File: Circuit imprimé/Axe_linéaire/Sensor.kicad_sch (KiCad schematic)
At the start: 0 parts

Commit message: Ajout de l'IMU + modèle du photointerrupteur
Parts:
- added C1, C2: 100n, symbol Device:C
- added JP1: SolderJumper_3_Bridged12, symbol Jumper:SolderJumper_3_Bridged12
- added JP2: SolderJumper_2_Open, symbol Jumper:SolderJumper_2_Open
- added R1: 10k, symbol Device:R
- added U2: LSM6DSRTR, Library:LGA-14_2.5X3X0.86_, symbol 2022-12-24_18-31-24:LSM6DSRTR
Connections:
- new net: JP2.1 (A), R1.2, U2.1 (SDO/SA0)
- new net: JP1.2 (C), U2.12 (CS)
- new net +3.3V: C1.1, C2.1, JP1.1 (A), R1.1, U2.5 (VDD_IO), U2.8 (VDD)
- new net GND: C1.2, C2.2, JP2.2 (B), U2.2 (SDX_), U2.3 (SCX), U2.6 (GND), U2.7 (GND)
- new net INT1_Bas: U2.4 (INT1)
- new net INT2_Bas: U2.9 (INT2)
- new net SCL: U2.13 (SCL)
- new net SDA: U2.14 (SDA)

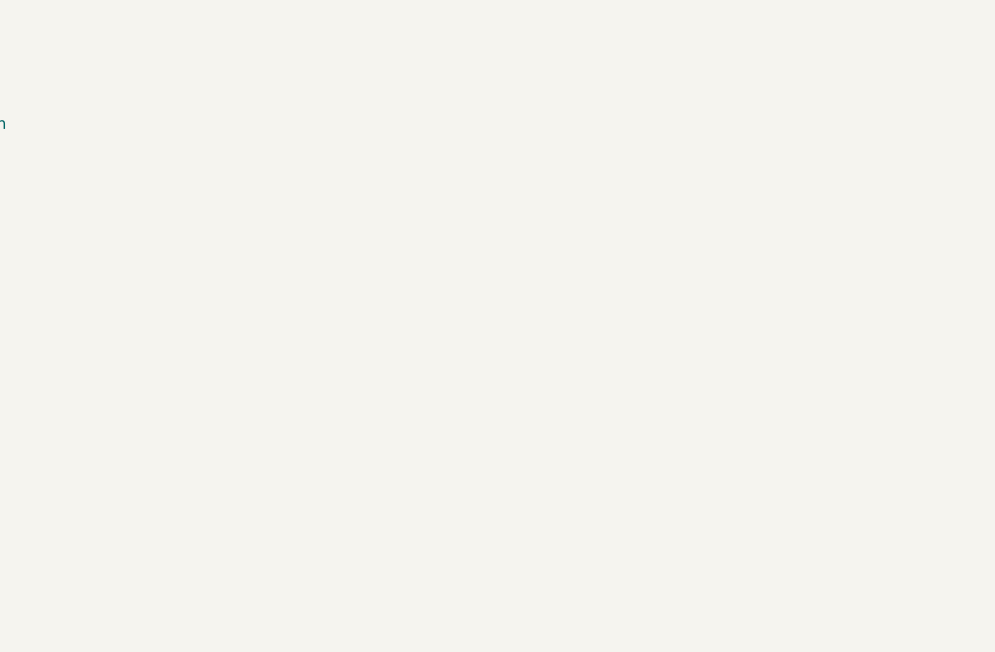
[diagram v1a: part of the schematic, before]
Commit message: ajout du circuit de position + carte SD
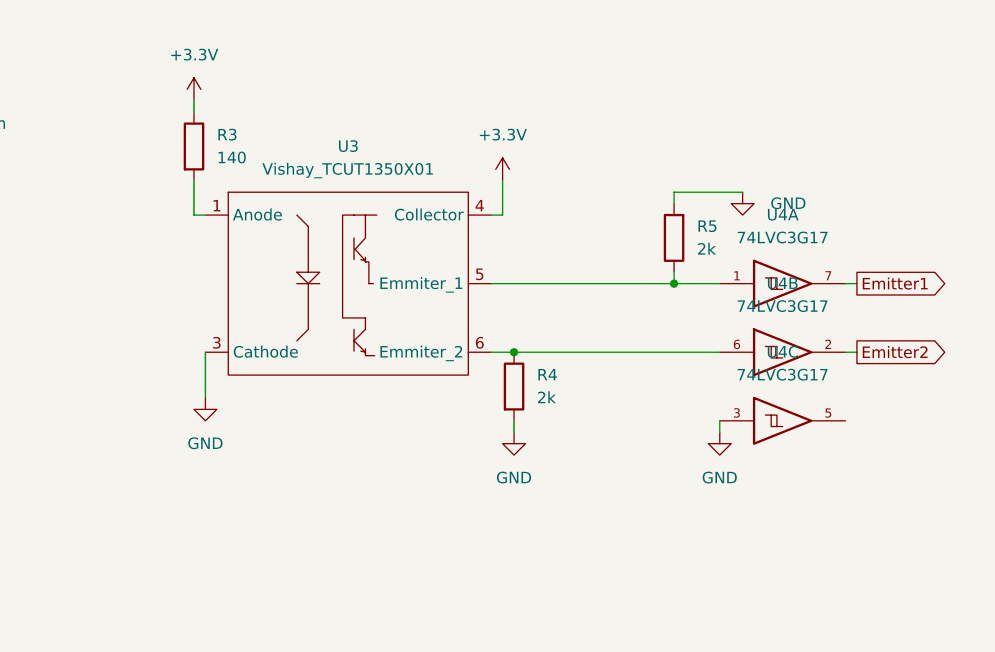
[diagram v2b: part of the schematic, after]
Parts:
- added R3: 140, symbol Device:R
- added R4, R5: 2k, symbol Device:R
- added U3: Vishay_TCUT1350X01, Library:Vishay TCUT1350X01, symbol Library:Vishay_TCUT1350X01
- added U4: 74LVC3G17, symbol 74xGxx:74LVC3G17
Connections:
- net +3.3V: now also R3.1, U3.4 (Collector)
- net GND: now also R4.2, R5.2, U3.3 (Cathode), U4.3, U4.4 (GND), U4.4 (GND), U4.4 (GND)
- new net: R3.2, U3.1 (Anode)
- new net: R5.1, U3.5 (Emmiter_1), U4.1
- new net: R4.1, U3.6 (Emmiter_2), U4.6
- new net Emitter1: U4.7
- new net Emitter2: U4.2
- new net VCC: U4.8 (VCC), U4.8 (VCC), U4.8 (VCC)

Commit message: circuit V1
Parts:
- added R10, R11: 1k, Resistor_SMD:R_0603_1608Metric, symbol Device:R
- added R12: 30, Resistor_SMD:R_0805_2012Metric, symbol Device:R
- added TP1, TP2, TP3: TestPoint, TestPoint:TestPoint_Pad_D2.0mm, symbol Connector:TestPoint
- C1, C2: footprint (none) -> Library:Cap 100nf 0805
- JP1: footprint (none) -> Jumper:SolderJumper-3_P1.3mm_Bridged12_RoundedPad1.0x1.5mm
- JP2: footprint (none) -> Jumper:SolderJumper-2_P1.3mm_Open_RoundedPad1.0x1.5mm
- R1: footprint (none) -> Resistor_SMD:R_0603_1608Metric
- R3: value 140 -> 100; footprint (none) -> Resistor_SMD:R_0603_1608Metric
- R4, R5: value 2k -> 1k; footprint (none) -> Resistor_SMD:R_0603_1608Metric
- U4: footprint (none) -> Package_SO:VSSOP-8_2.3x2mm_P0.5mm
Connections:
- net +3.3V: now also R12.1; no longer R3.1
- net GND: now also R10.2, R11.1; no longer R4.2, R5.2
- net at R5.1, U3.5 (Emmiter_1), U4.1: now also TP2.1
- net at R4.1, U3.6 (Emmiter_2), U4.6: now also TP3.1
- net at JP1.2 (C), U2.12 (CS): now also TP1.1
- net VCC renamed +3V3
- new net: R11.2, R5.2
- new net: R10.1, R4.2
- new net: R12.2, R3.1
- no-connect marks 0 -> 3
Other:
- moved on the sheet: U4A, U4C

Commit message: tout mes CI sont pret
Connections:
- net +3V3 is gone; now on net +3.3V: U4.8 (+3.3V), U4.8 (+3.3V), U4.8 (+3.3V)
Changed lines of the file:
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@@
-    (stroke (width 0) (type default) (color 0 0 0 0))
-  )
-  (wire (pts (xy 207.01 50.8) (xy 207.01 54.61))
     (stroke (width 0) (type default) (color 0 0 0 0))
   )
@@
     (pin "1")
   )
-  (symbol (lib_id "74xGxx:74LVC3G17") (at 207.01 57.15 0) (unit 2)
+  (symbol (lib_name "74LVC3G17_2") (lib_id "74xGxx:74LVC3G17") (at 207.01 57.15 0) (unit 2)
     (in_bom yes) (on_board yes)
     (property "Reference" "U4" (id 0) (at 208.915 43.18 0))
@@
     (pin "1")
   )
-  (symbol (lib_id "power:+3V3") (at 207.01 50.8 0) (unit 1)
-    (in_bom yes) (on_board yes) (fields_autoplaced)
-    (property "Reference" "#PWR0106" (id 0) (at 207.01 54.61 0)
-      (effects (font (size 1.27 1.27)) hide)
-    )
-    (property "Value" "+3V3" (id 1) (at 207.01 45.72 0))
-    (property "Footprint" "" (id 2) (at 207.01 50.8 0)
-      (effects (font (size 1.27 1.27)) hide)
-    )
-    (property "Datasheet" "" (id 3) (at 207.01 50.8 0)
-      (effects (font (size 1.27 1.27)) hide)
-    )
-    (pin "1")
-  )
   (symbol (lib_id "Connector:TestPoint") (at 186.69 49.53 0) (unit 1)
     (in_bom yes) (on_board yes) (fields_autoplaced)
@@
     (pin "2")
   )
-  (symbol (lib_id "74xGxx:74LVC3G17") (at 209.55 43.18 0) (unit 1)
+  (symbol (lib_name "74LVC3G17_1") (lib_id "74xGxx:74LVC3G17") (at 209.55 43.18 0) (unit 1)
     (in_bom yes) (on_board yes) (fields_autoplaced)
     (property "Reference" "U4" (id 0) (at 208.915 35.56 0))
